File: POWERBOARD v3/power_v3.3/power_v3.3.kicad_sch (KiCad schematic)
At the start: 0 parts

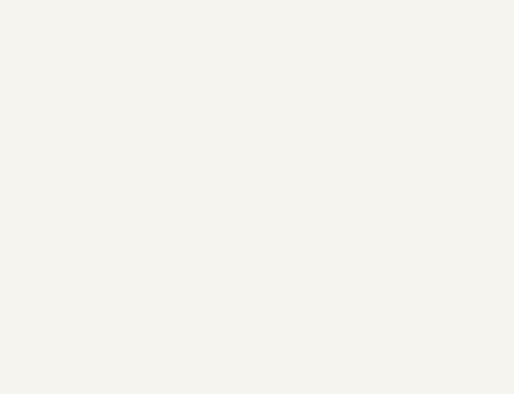
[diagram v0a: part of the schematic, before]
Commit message: updated routing, added mounting holes
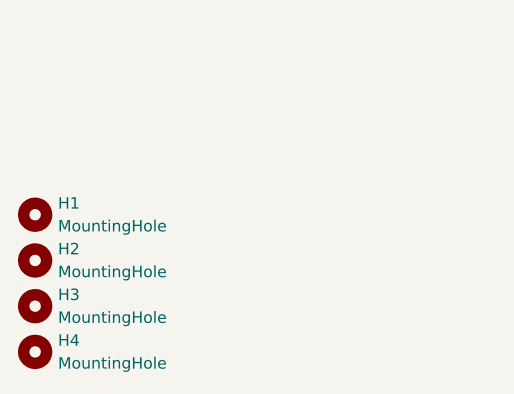
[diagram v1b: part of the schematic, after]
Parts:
- added H1, H2, H3, H4: MountingHole, MountingHole:MountingHole_2.2mm_M2_DIN965_Pad, symbol Mechanical:MountingHole

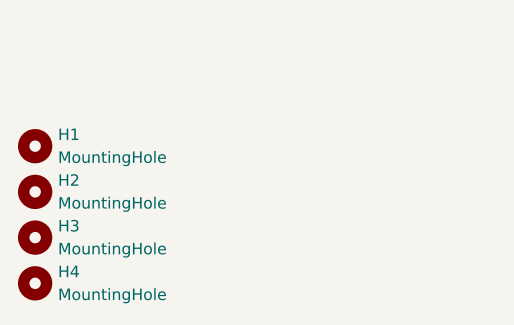
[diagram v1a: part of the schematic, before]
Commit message: added .stp files and extra layout changes, 1 extra mounting hole
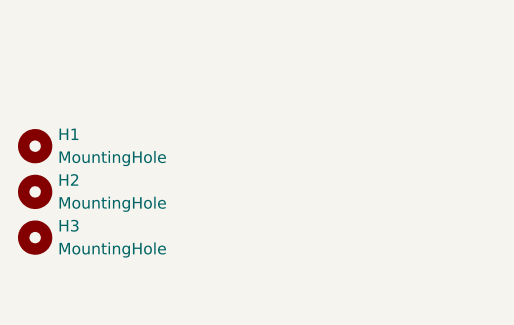
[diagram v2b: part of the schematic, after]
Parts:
- removed H4: MountingHole, MountingHole:MountingHole_2.2mm_M2_DIN965_Pad, symbol Mechanical:MountingHole
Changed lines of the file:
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@@
+	(symbol
+		(lib_id "Mechanical:MountingHole")
+		(at 30.48 173.99 0)
+		(unit 1)
+		(body_style 1)
+		(exclude_from_sim no)
+		(in_bom no)
+		(on_board yes)
+		(in_pos_files yes)
+		(dnp no)
+		(fields_autoplaced yes)
+		(property "Reference" "H3"
+			(at 33.02 172.7199 0)
+			(show_name no)
+			(do_not_autoplace no)
+			(effects
+				(font
+					(size 1.27 1.27)
+				)
+				(justify left)
+			)
+		)
+		(property "Value" "MountingHole"
+			(at 33.02 175.2599 0)
+			(show_name no)
+			(do_not_autoplace no)
+			(effects
+				(font
+					(size 1.27 1.27)
+				)
+				(justify left)
+			)
+		)
+		(property "Footprint" "MountingHole:MountingHole_2.2mm_M2_DIN965_Pad"
+			(at 30.48 173.99 0)
+			(hide yes)
+			(show_name no)
+			(do_not_autoplace no)
+			(effects
+				(font
+					(size 1.27 1.27)
+				)
+			)
+		)
+		(property "Datasheet" ""
+			(at 30.48 173.99 0)
+			(hide yes)
+			(show_name no)
+			(do_not_autoplace no)
+			(effects
+				(font
+					(size 1.27 1.27)
+				)
+			)
+		)
+		(property "Description" "Mounting Hole without connection"
+			(at 30.48 173.99 0)
+			(hide yes)
+			(show_name no)
+			(do_not_autoplace no)
+			(effects
+				(font
+					(size 1.27 1.27)
+				)
+			)
+		)
+		(instances
+			(project "power_v3.3"
+				(path "/432bcdcf-747a-4fa0-b87b-096f44260199"
+					(reference "H3")
+					(unit 1)
+				)
+			)
+		)
+	)
 	(symbol
 		(lib_id "Mechanical:MountingHole")
@@
 					(unit 1)
 				)
-			)
-		)
-	)
-	(symbol
-		(lib_id "Mechanical:MountingHole")
-		(at 30.48 173.99 0)
-		(unit 1)
-		(body_style 1)
-		(exclude_from_sim no)
-		(in_bom no)
-		(on_board yes)
-		(in_pos_files yes)
-		(dnp no)
-		(fields_autoplaced yes)
-		(property "Reference" "H3"
-			(at 33.02 172.7199 0)
-			(show_name no)
-			(do_not_autoplace no)
-			(effects
-				(font
-					(size 1.27 1.27)
-				)
-				(justify left)
-			)
-		)
-		(property "Value" "MountingHole"
-			(at 33.02 175.2599 0)
-			(show_name no)
-			(do_not_autoplace no)
-			(effects
-				(font
-					(size 1.27 1.27)
-				)
-				(justify left)
-			)
-		)
-		(property "Footprint" "MountingHole:MountingHole_2.2mm_M2_DIN965_Pad"
-			(at 30.48 173.99 0)
-			(hide yes)
-			(show_name no)
-			(do_not_autoplace no)
-			(effects
-				(font
-					(size 1.27 1.27)
-				)
-			)
-		)
-		(property "Datasheet" ""
-			(at 30.48 173.99 0)
-			(hide yes)
-			(show_name no)
-			(do_not_autoplace no)
-			(effects
-				(font
-					(size 1.27 1.27)
-				)
-			)
-		)
-		(property "Description" "Mounting Hole without connection"
-			(at 30.48 173.99 0)
-			(hide yes)
-			(show_name no)
-			(do_not_autoplace no)
-			(effects
-				(font
-					(size 1.27 1.27)
-				)
-			)
-		)
-		(instances
-			(project "power_v3.3"
-				(path "/432bcdcf-747a-4fa0-b87b-096f44260199"
-					(reference "H3")
-					(unit 1)
-				)
-			)
-		)
-	)
-	(symbol
-		(lib_id "Mechanical:MountingHole")
-		(at 30.48 179.07 0)
-		(unit 1)
-		(body_style 1)
-		(exclude_from_sim no)
-		(in_bom no)
-		(on_board yes)
-		(in_pos_files yes)
-		(dnp no)
-		(fields_autoplaced yes)
-		(property "Reference" "H4"
-			(at 33.02 177.7999 0)
-			(show_name no)
-			(do_not_autoplace no)
-			(effects
-				(font
-					(size 1.27 1.27)
-				)
-				(justify left)
-			)
-		)
-		(property "Value" "MountingHole"
-			(at 33.02 180.3399 0)
-			(show_name no)
-			(do_not_autoplace no)
-			(effects
-				(font
-					(size 1.27 1.27)
-				)
-				(justify left)
-			)
-		)
-		(property "Footprint" "MountingHole:MountingHole_2.2mm_M2_DIN965_Pad"
-			(at 30.48 179.07 0)
-			(hide yes)
-			(show_name no)
-			(do_not_autoplace no)
-			(effects
-				(font
-					(size 1.27 1.27)
-				)
-			)
-		)
-		(property "Datasheet" ""
-			(at 30.48 179.07 0)
-			(hide yes)
-			(show_name no)
-			(do_not_autoplace no)
-			(effects
-				(font
-					(size 1.27 1.27)
-				)
-			)
-		)
-		(property "Description" "Mounting Hole without connection"
-			(at 30.48 179.07 0)
-			(hide yes)
-			(show_name no)
-			(do_not_autoplace no)
-			(effects
-				(font
-					(size 1.27 1.27)
-				)
-			)
-		)
-		(instances
-			(project "power_v3.3"
-				(path "/432bcdcf-747a-4fa0-b87b-096f44260199"
-					(reference "H4")
-					(unit 1)
-				)
